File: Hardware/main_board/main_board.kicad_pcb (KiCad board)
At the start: 6 copper layers, 95.4 x 36.1 mm, 232 parts, among them J1 BATT, J2 LCD, J3 BACK_LIGHT, J4 SD, J5 NFC, J6 EXT1, J7 EXT0, J8 USB_C, Q1 DMN313DLT, SW1 OK, SW2 BACK, SW3 RIGHT, SW4 LEFT, SW5 UP, SW6 DOWN, T1 B0310J50100AHF, U1 STM32WB55RGVx, U10 BGS13S4N9E6327XTSA1, U11 NC7SZ32M5X, U12 LP5562TMX, U2 BQ27220YZFR, U3 BQ25896RTWR, U4 RS3221-3.3YF3, U5 LM66100DCK, U6 LM3281YFQR, U7 LM3281YFQR, U8 CC1101RGP, U9 BGS13S4N9E6327XTSA1, Y1 32MHz, Y2 32.768K, Y3 26MHz

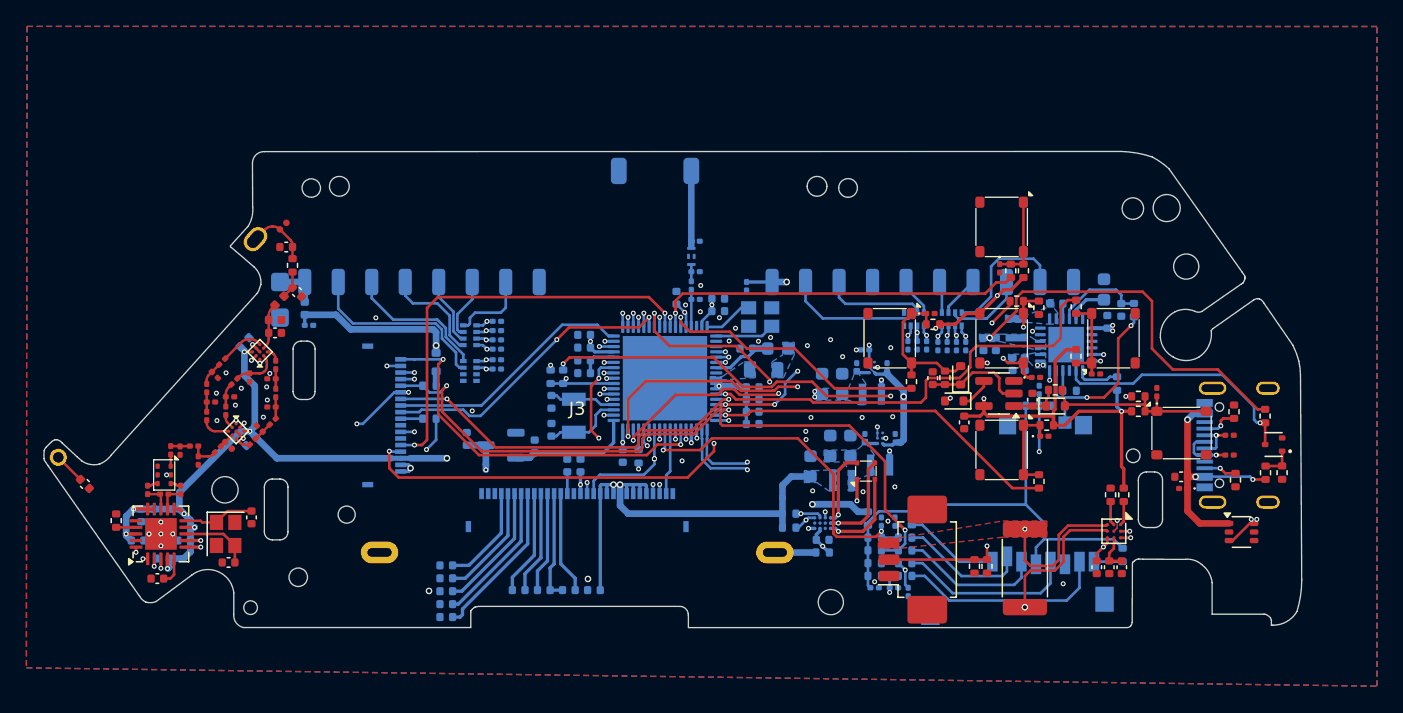
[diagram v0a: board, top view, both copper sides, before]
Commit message: layout: cleanup tracks and vias
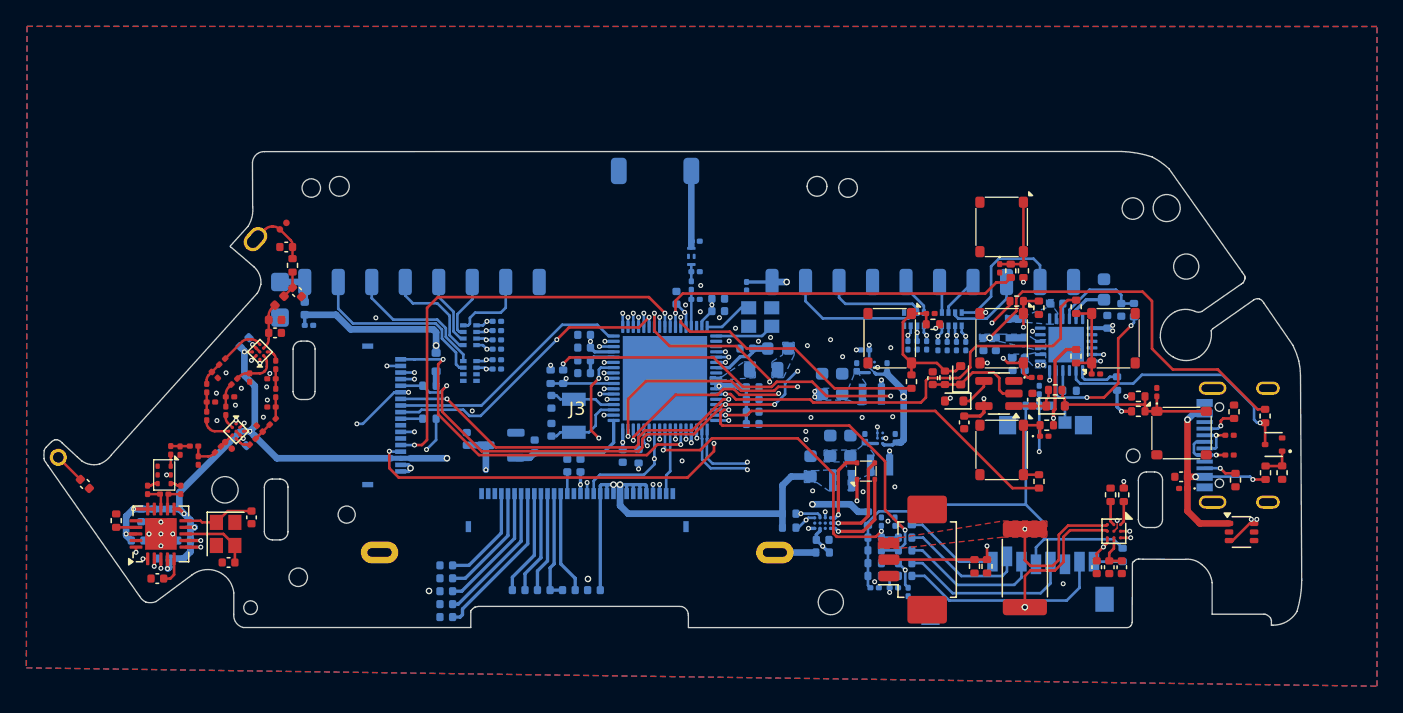
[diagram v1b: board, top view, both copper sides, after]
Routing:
- net +3.3V: track 141.7 -> 116.6 mm, vias 24 -> 27
- net /LCD/SPI_D_SCK: vias 3 -> 2

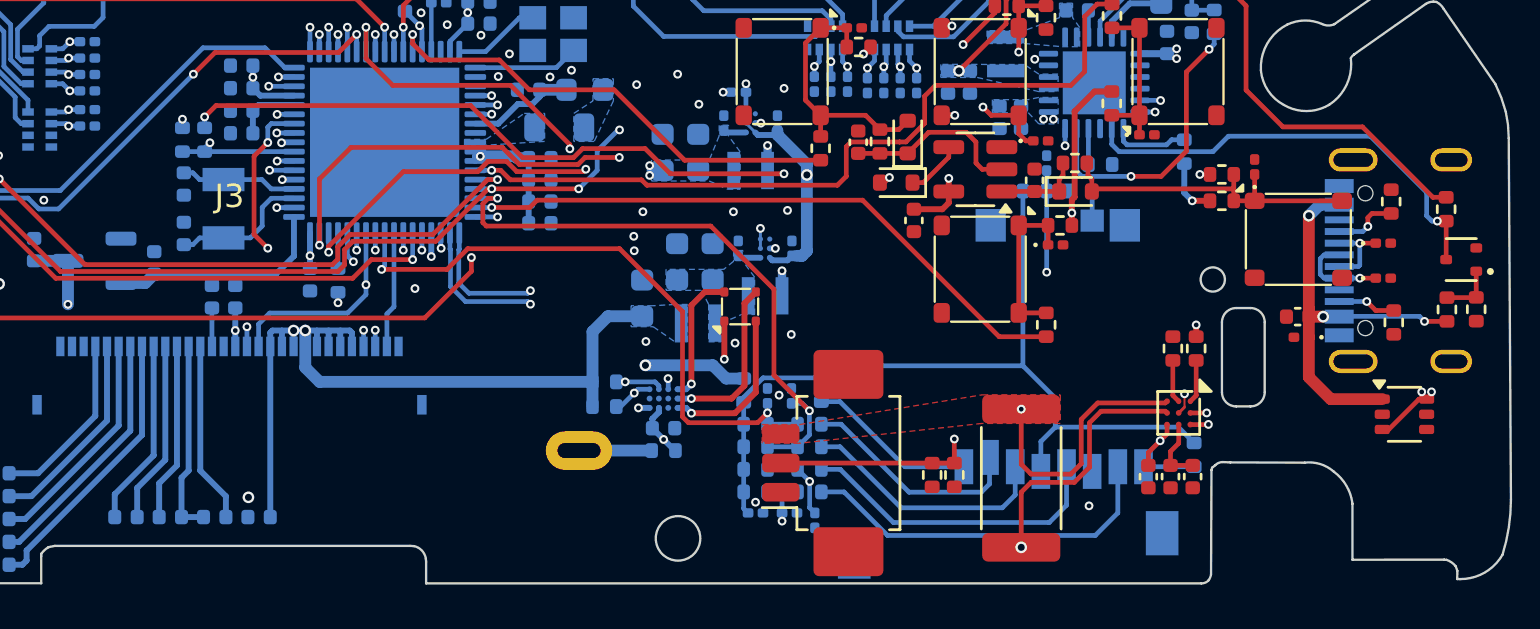
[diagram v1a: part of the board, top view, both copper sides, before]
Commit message: layout: add some testpoints
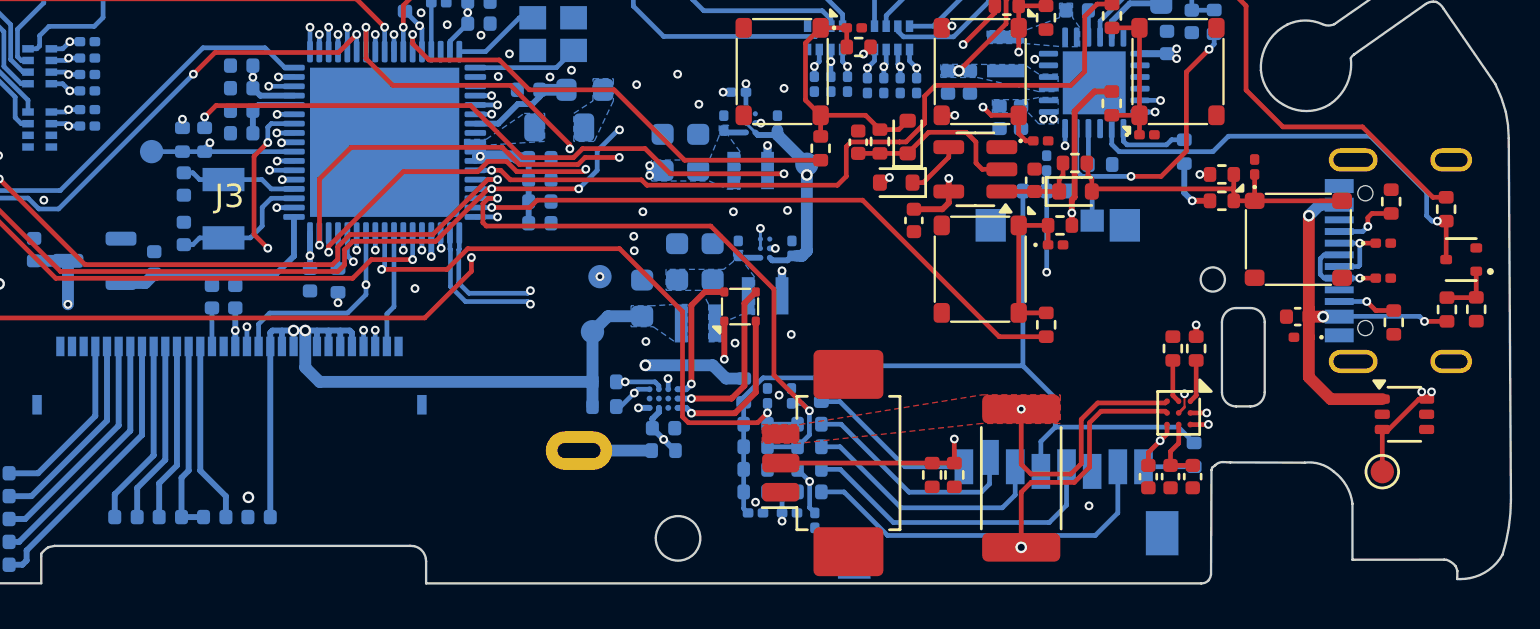
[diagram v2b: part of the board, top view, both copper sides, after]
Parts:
- added TP1: RST, TestPoint:TestPoint_Pad_D1.0mm, B.Cu at (143.7, 106.5)
- added TP12: 5V_USB, TestPoint:TestPoint_Pad_D1.0mm, F.Cu at (196.5, 120.2)
- added TP18: VSYS, TestPoint:TestPoint_Pad_D1.0mm, B.Cu at (171.8, 107.0)
- added TP20: 3V3_MAIN, TestPoint:TestPoint_Pad_D1.0mm, B.Cu at (162.6, 114.2)
- added TP21: 3V3_EXT, TestPoint:TestPoint_Pad_D1.0mm, B.Cu at (162.9, 111.8)
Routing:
- net VUSB: track 116.3 -> 118.2 mm
- net /Buttons/RESET: track 29.7 -> 31.0 mm
- net +3.3V_EXT: vias 4 -> 5

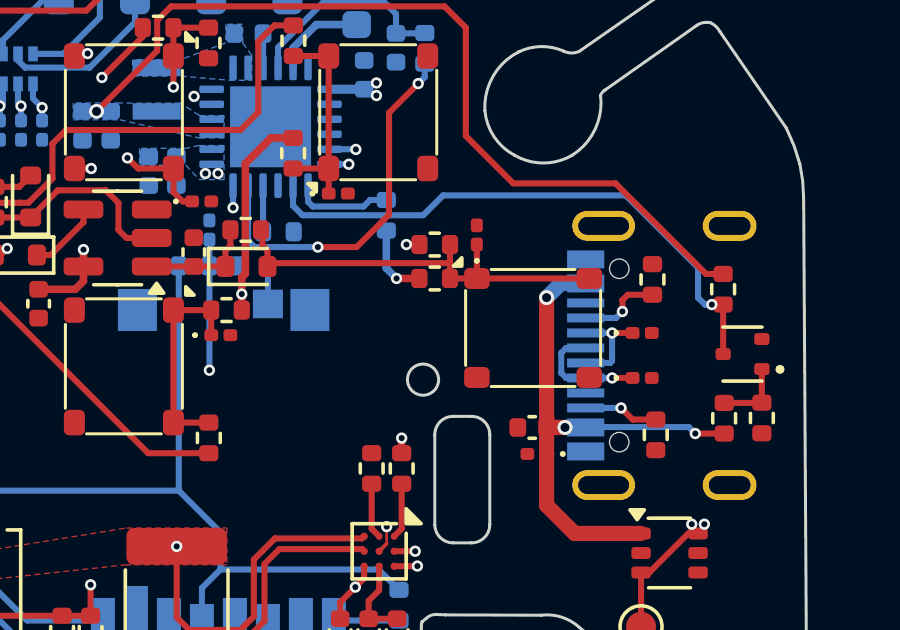
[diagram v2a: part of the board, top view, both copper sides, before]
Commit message: layout: move the back button
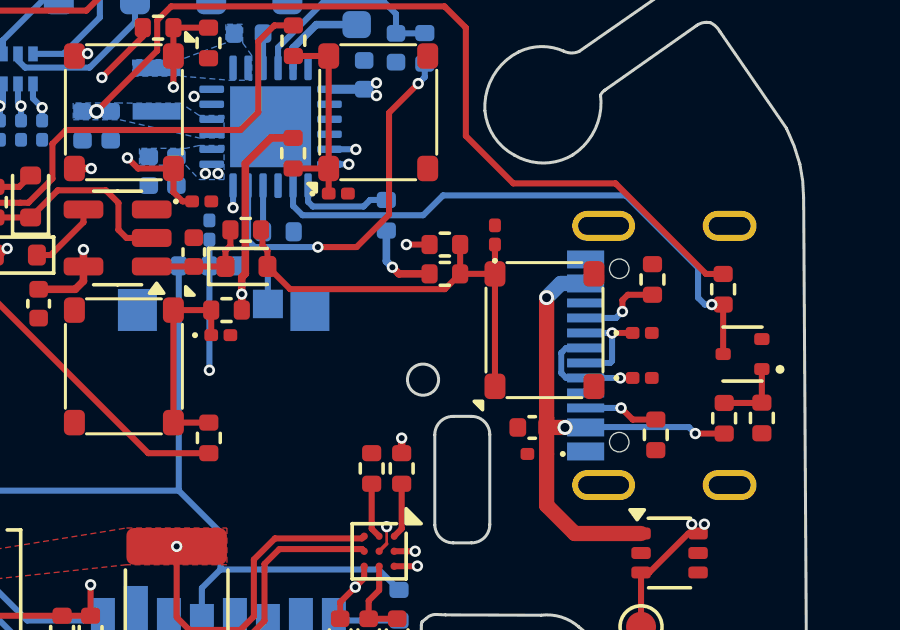
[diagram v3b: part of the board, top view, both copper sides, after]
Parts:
- moved D2 0.60 mm to (191.6, 107.1)
- moved SW2 0.38 mm to (193.2, 110.3), turned to 90 degrees
- moved R19 0.37 mm to (189.9, 108.4)
- moved R25 0.34 mm to (189.9, 107.5)
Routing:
- net /Buttons/BACK: track 14.0 -> 15.1 mm
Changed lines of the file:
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@@
 	(footprint "Diode_SMD:D_0201_0603Metric"
 		(layer "F.Cu")
-		(at 190.996976 107.138559 90)
+		(at 191.6 107.138559 90)
 		(descr "Diode SMD 0201 (0603 Metric), square (rectangular) end terminal, IPC_7351 nominal, (Body size source: https://www.vishay.com/docs/20052/crcw0201e3.pdf), generated with kicad-footprint-generator")
 		(tags "diode")
@@
 	(footprint "Resistor_SMD:R_0402_1005Metric"
 		(layer "F.Cu")
-		(at 189.591976 107.458559)
+		(at 189.93 107.458559)
 		(descr "Resistor SMD 0402 (1005 Metric), square (rectangular) end terminal, IPC_7351 nominal, (Body size source: IPC-SM-782 page 72, https://www.pcb-3d.com/wordpress/wp-content/uploads/ipc-sm-782a_amendment_1_and_2.pdf), generated with kicad-footprint-generator")
 		(tags "resistor")
@@
 	(footprint "Library:SW_Push_SPST_NO_Alps_ SKRM"
 		(layer "F.Cu")
-		(at 192.871976 110.238559)
+		(at 193.25 110.31 90)
 		(property "Reference" "SW2"
-			(at 0 -12.652 0)
+			(at 0 -12.652 90)
 			(unlocked yes)
 			(layer "F.SilkS")
@@
 		)
 		(property "Value" "BACK"
-			(at 0 -11.152 0)
+			(at 0 -11.152 90)
 			(unlocked yes)
 			(layer "F.Fab")
@@
 		)
 		(property "Footprint" "Library:SW_Push_SPST_NO_Alps_ SKRM"
-			(at 0 -12.152 0)
+			(at 0 -12.152001 90)
 			(unlocked yes)
 			(layer "F.Fab")
@@
 		)
 		(property "Datasheet" ""
-			(at 0 -12.152 0)
+			(at 0 -12.152001 90)
 			(unlocked yes)
 			(layer "F.Fab")
@@
 		)
 		(property "Description" "Push button switch, generic, two pins"
-			(at 0 -12.152 0)
+			(at 0 -12.152001 90)
 			(unlocked yes)
 			(layer "F.Fab")
@@
 		(attr smd)
 		(fp_line
-			(start -2.25 -1.25)
-			(end -2.25 1.25)
+			(start -1.4 -1.95)
+			(end 1.4 -1.95)
 			(stroke
 				(width 0.1)
@@
 		)
 		(fp_line
-			(start -1.4 -1.95)
-			(end 1.4 -1.95)
+			(start 2.25 -1.25)
+			(end 2.25 1.25)
 			(stroke
 				(width 0.1)
@@
 		)
 		(fp_line
-			(start -1.4 1.95)
-			(end 1.4 1.95)
+			(start -2.25 -1.25)
+			(end -2.25 1.25)
 			(stroke
 				(width 0.1)
@@
 		)
 		(fp_line
-			(start 2.25 -1.25)
-			(end 2.25 1.25)
+			(start -1.4 1.95)
+			(end 1.4 1.95)
 			(stroke
 				(width 0.1)
@@
 		(fp_poly
 			(pts
-				(xy -2.375 -2.061765) (xy -2.655 -2.061765) (xy -2.375 -2.341765) (xy -2.375 -2.061765)
+				(xy -2.375001 -2.061765) (xy -2.655 -2.061766) (xy -2.375001 -2.341765) (xy -2.375001 -2.061765)
 			)
 			(stroke
@@
 			(layer "F.SilkS")
 		)
-		(fp_rect
-			(start -2.35 -2.35)
-			(end 2.35 2.35)
+		(fp_poly
+			(pts
+				(xy -2.35 -2.35) (xy 2.35 -2.35) (xy 2.35 2.35) (xy -2.35 2.35)
+			)
 			(stroke
 				(width 0.05)
@@
 		)
 		(fp_text user "${REFERENCE}"
-			(at 0 -9.652 0)
+			(at 0 -9.652 90)
 			(unlocked yes)
 			(layer "F.Fab")
@@
 		)
 		(pad "1" smd roundrect
-			(at -1.875 -1.65)
+			(at -1.875 -1.65 90)
 			(size 0.85 0.7)
 			(layers "F.Cu" "F.Paste" "F.Mask")
@@
 		)
 		(pad "1" smd roundrect
-			(at 1.875 -1.65)
+			(at 1.875 -1.65 90)
 			(size 0.85 0.7)
 			(layers "F.Cu" "F.Paste" "F.Mask")
@@
 		)
 		(pad "2" smd roundrect
-			(at -1.875 1.65)
+			(at -1.875 1.65 90)
 			(size 0.85 0.7)
 			(layers "F.Cu" "F.Paste" "F.Mask")
@@
 		)
 		(pad "2" smd roundrect
-			(at 1.875 1.65)
+			(at 1.875 1.65 90)
 			(size 0.85 0.7)
 			(layers "F.Cu" "F.Paste" "F.Mask")
@@
 	(footprint "Resistor_SMD:R_0402_1005Metric"
 		(layer "F.Cu")
-		(at 189.591977 108.588559 180)
+		(at 189.93 108.435 180)
 		(descr "Resistor SMD 0402 (1005 Metric), square (rectangular) end terminal, IPC_7351 nominal, (Body size source: IPC-SM-782 page 72, https://www.pcb-3d.com/wordpress/wp-content/uploads/ipc-sm-782a_amendment_1_and_2.pdf), generated with kicad-footprint-generator")
 		(tags "resistor")
@@
 	)
 	(segment
+		(start 188.1818 108.215)
+		(end 188.4018 108.435)
+		(width 0.254)
+		(layer "F.Cu")
+		(net 4)
+	)
+	(segment
 		(start 184.13244 103.90356)
 		(end 184.871976 103.90356)
@@
 	)
 	(segment
-		(start 177.884476 108.188559)
-		(end 177.884476 107.626976)
+		(start 188.4018 108.435)
+		(end 189.42 108.435)
 		(width 0.254)
 		(layer "F.Cu")
@@
 	)
 	(segment
-		(start 117.234027 116.351924)
-		(end 116.881527 115.999424)
+		(start 177.884476 108.188559)
+		(end 177.884476 107.626976)
 		(width 0.254)
 		(layer "F.Cu")
@@
 	)
 	(segment
-		(start 188.32 108.588559)
-		(end 189.081977 108.588559)
+		(start 117.234027 116.351924)
+		(end 116.881527 115.999424)
 		(width 0.254)
 		(layer "F.Cu")
@@
 	)
 	(via
-		(at 188.32 108.588559)
+		(at 188.1818 108.215)
 		(size 0.3778)
 		(drill 0.2)
@@
 	)
 	(segment
-		(start 187.98 106.991923)
-		(end 187.98 108.248559)
-		(width 0.254)
-		(layer "B.Cu")
-		(net 4)
-	)
-	(segment
 		(start 151.796861 114.831924)
 		(end 151.796861 114.15)
@@
 	)
 	(segment
-		(start 187.98 108.248559)
-		(end 188.32 108.588559)
-		(width 0.254)
-		(layer "B.Cu")
-		(net 4)
-	)
-	(segment
 		(start 150.5 110.9464)
 		(end 150.5 109.9675)
@@
 	)
 	(segment
+		(start 187.98 108.0132)
+		(end 187.98 106.991923)
+		(width 0.254)
+		(layer "B.Cu")
+		(net 4)
+	)
+	(segment
 		(start 159.39 106.76)
 		(end 159.8735 106.76)
@@
 	)
 	(segment
+		(start 188.1818 108.215)
+		(end 187.98 108.0132)
+		(width 0.254)
+		(layer "B.Cu")
+		(net 4)
+	)
+	(segment
 		(start 121.814145 104.015092)
 		(end 121.814145 105.875092)
@@
 	)
 	(segment
+		(start 191.6 108.435)
+		(end 191.6 107.458559)
+		(width 0.2032)
+		(layer "F.Cu")
+		(net 57)
+	)
+	(segment
 		(start 184.016976 108.188558)
 		(end 184.016976 107.663024)
@@
 	)
 	(segment
-		(start 190.996976 108.588559)
-		(end 194.746976 108.588559)
+		(start 190.44 108.435)
+		(end 191.6 108.435)
 		(width 0.2032)
 		(layer "F.Cu")
@@
 	)
 	(segment
-		(start 190.101977 108.588559)
-		(end 190.101977 108.08)
+		(start 190.44 107.458559)
+		(end 190.44 108.435)
 		(width 0.2032)
 		(layer "F.Cu")
@@
 	)
 	(segment
-		(start 190.996976 108.588559)
-		(end 190.101977 108.588559)
+		(start 184.773918 108.9455)
+		(end 189.9295 108.9455)
 		(width 0.2032)
 		(layer "F.Cu")
@@
 	)
 	(segment
-		(start 184.127475 108.078059)
-		(end 190.100036 108.078059)
+		(start 191.6 112.185)
+		(end 191.6 108.435)
 		(width 0.2032)
 		(layer "F.Cu")
@@
 	)
 	(segment
-		(start 190.101977 108.08)
-		(end 190.101977 107.61856)
+		(start 189.9295 108.9455)
+		(end 190.44 108.435)
 		(width 0.2032)
 		(layer "F.Cu")
@@
 	)
 	(segment
-		(start 190.996976 108.588559)
-		(end 190.996976 107.458559)
+		(start 184.016976 108.188558)
+		(end 184.773918 108.9455)
 		(width 0.2032)
 		(layer "F.Cu")
@@
 	(segment
 		(start 196.188477 111.905124)
-		(end 195.504876 111.905124)
+		(end 195.78 111.905124)
 		(width 0.2)
 		(layer "F.Cu")
@@
 	)
 	(via
-		(at 195.504876 111.905124)
+		(at 195.78 111.905124)
 		(size 0.3778)
 		(drill 0.2)
@@
 	)
 	(segment
-		(start 186.8478 111.333648)
-		(end 187.133648 111.0478)
-		(width 0.20066)
+		(start 195.78 111.905124)
+		(end 195.187324 111.905124)
+		(width 0.2)
 		(layer "In4.Cu")
 		(net 88)
 	)
 	(segment
-		(start 195.504876 111.905124)
-		(end 195.187324 111.905124)
-		(width 0.2)
+		(start 186.8478 111.333648)
+		(end 187.133648 111.0478)
+		(width 0.20066)
 		(layer "In4.Cu")
 		(net 88)
@@
 	)
 	(segment
-		(start 193.975473 111.905124)
-		(end 194.623273 111.905124)
+		(start 194.623273 111.905124)
+		(end 195.78 111.905124)
 		(width 0.2)
 		(layer "B.Cu")
@@
 	)
 	(segment
-		(start 194.623273 111.905124)
-		(end 195.504876 111.905124)
+		(start 193.975473 111.905124)
+		(end 194.623273 111.905124)
 		(width 0.2)
 		(layer "B.Cu")
@@
 	)
 	(segment
-		(start 189.081976 107.458559)
+		(start 189.42 107.458559)
 		(end 188.648559 107.458559)
 		(width 0.2032)
